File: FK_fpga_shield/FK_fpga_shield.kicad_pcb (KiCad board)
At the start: 2 copper layers, 136 parts, among them J0 USB_B_Mini, J1 molex-51382-0400-microclasp, J10 molex-51382-0400-microclasp, J11 molex-51382-0400-microclasp, J12 molex-51382-0400-microclasp, J13 molex-51382-0400-microclasp, J14 molex-51382-0400-microclasp, J15 molex-51382-0400-microclasp, J16 molex-51382-0400-microclasp, J17 molex-51382-0400-microclasp, J18 molex-51382-0400-microclasp, J19 molex-51382-0400-microclasp, J2 molex-51382-0400-microclasp, J20 molex-51382-0400-microclasp, J21 molex-51382-0400-microclasp, J22 molex-51382-0400-microclasp, J23 molex-51382-0400-microclasp, J24 molex-51382-0400-microclasp, J25 molex-51382-0400-microclasp, J26 molex-51382-0400-microclasp, J27 molex-51382-0400-microclasp, J28 molex-51382-0400-microclasp, J29 molex-51382-0400-microclasp, J3 molex-51382-0400-microclasp, J30 molex-51382-0400-microclasp, J31 molex-51382-0400-microclasp, J32 molex-51382-0400-microclasp, J33 molex-51382-0400-microclasp, J34 molex-51382-0400-microclasp, J35 molex-51382-0400-microclasp, J4 molex-51382-0400-microclasp, J5 molex-51382-0400-microclasp, J6 molex-51382-0400-microclasp, J7 molex-51382-0400-microclasp, J8 molex-51382-0400-microclasp, J9 molex-51382-0400-microclasp, U1 FT232RL, U2 nvt2010pw, U3 nvt2010pw, U4 nvt2010pw, U5 nvt2010pw, U6 nvt2010pw, U7 nvt2010pw, U8 nvt2010pw

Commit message: wip lazyour (mapped to header)
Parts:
- removed the J11 at (221.2, 43.8)
- added J15: molex-51382-0400-microclasp, FK_fpga_shield_custom_footprints:Molex_MicroClasp_55935-0410_1x04_P2.00mm_Horizontal_3DMODEL, F.Cu at (247.0, 65.2)
- moved C6 349.4 mm to (345.1, 24.9)
- moved R79 349.4 mm to (349.9, 33.7)
- moved C2 349.4 mm to (360.3, 55.8)
- moved C4 349.4 mm to (365.1, 55.8)
- moved C7 349.4 mm to (334.1, 35.7)
- moved C8 349.4 mm to (329.4, 38.6)
- moved R54 349.4 mm to (348.4, 36.6)
- moved C9 298.0 mm to (345.2, -20.8)
- moved R53 298.0 mm to (345.2, -26.7)
- moved U4 274.0 mm to (214.4, 68.4), turned to 45 degrees
- moved C10 263.0 mm to (293.4, 9.55)
- moved C11 263.0 mm to (288.6, 12.5)
- moved C5 263.0 mm to (293.4, 15.4)
- moved R55 263.0 mm to (293.4, 21.4)
- moved R57 263.0 mm to (302.9, 17.1)
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- renumbered J15 to J11, J14 to J12, J12 to J14
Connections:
- H1 pad 13: Net-(H1-Pad13) -> /6b
- H1 pad 14: Net-(H1-Pad14) -> /6a
- H1 pad 15: Net-(H1-Pad15) -> /7b
- H1 pad 16: Net-(H1-Pad16) -> /7a
- H1 pad 17: Net-(H1-Pad17) -> /8b
- H1 pad 18: Net-(H1-Pad18) -> /8a
- H1 pad 19: Net-(H1-Pad19) -> /9b
- H1 pad 20: Net-(H1-Pad20) -> /9a
- H1 pad 21: Net-(H1-Pad21) -> /10b
- H1 pad 22: Net-(H1-Pad22) -> /10a
- H1 pad 23: Net-(H1-Pad23) -> /11b
- H1 pad 24: Net-(H1-Pad24) -> /11a
- H1 pad 25: Net-(H1-Pad25) -> /12b
- H1 pad 26: Net-(H1-Pad26) -> /12a
- H1 pad 27: Net-(H1-Pad27) -> /13b
- H1 pad 28: Net-(H1-Pad28) -> /13a
- H1 pad 31: Net-(H1-Pad31) -> /14b
- H1 pad 32: Net-(H1-Pad32) -> /14a
- H1 pad 33: Net-(H1-Pad33) -> /15b
- H1 pad 34: Net-(H1-Pad34) -> /15a
- H1 pad 35: Net-(H1-Pad35) -> /16b
- H1 pad 36: Net-(H1-Pad36) -> /16a
- H1 pad 37: Net-(H1-Pad37) -> /17b
- H1 pad 38: Net-(H1-Pad38) -> /17a
- H1 pad 39: Net-(H1-Pad39) -> /18b
- H1 pad 40: Net-(H1-Pad40) -> /18a
- H2 pad 1: Net-(H2-Pad1) -> /19b
- H2 pad 10: Net-(H2-Pad10) -> /23a
- H2 pad 13: Net-(H2-Pad13) -> /24b
- H2 pad 14: Net-(H2-Pad14) -> /24a
- H2 pad 15: Net-(H2-Pad15) -> /25b
- H2 pad 16: Net-(H2-Pad16) -> /25a
- H2 pad 17: Net-(H2-Pad17) -> /26b
- H2 pad 18: Net-(H2-Pad18) -> /26a
- H2 pad 19: Net-(H2-Pad19) -> /27b
- H2 pad 2: Net-(H2-Pad2) -> /19a
- H2 pad 20: Net-(H2-Pad20) -> /27a
- H2 pad 21: Net-(H2-Pad21) -> /28b
- H2 pad 22: Net-(H2-Pad22) -> /28a
- H2 pad 23: Net-(H2-Pad23) -> /29b
- H2 pad 24: Net-(H2-Pad24) -> /29a
- H2 pad 25: Net-(H2-Pad25) -> /30b
- H2 pad 26: Net-(H2-Pad26) -> /30a
- H2 pad 27: Net-(H2-Pad27) -> /31b
- H2 pad 28: Net-(H2-Pad28) -> /31a
- H2 pad 3: Net-(H2-Pad3) -> /20b
- H2 pad 31: Net-(H2-Pad31) -> /32b
- H2 pad 32: Net-(H2-Pad32) -> /32a
- H2 pad 33: Net-(H2-Pad33) -> /33b
- H2 pad 34: Net-(H2-Pad34) -> /33a
- H2 pad 35: Net-(H2-Pad35) -> /34b
- H2 pad 36: Net-(H2-Pad36) -> /34a
- H2 pad 37: Net-(H2-Pad37) -> /35b
- H2 pad 38: Net-(H2-Pad38) -> /35a
- H2 pad 39: Net-(H2-Pad39) -> /TX
- H2 pad 4: Net-(H2-Pad4) -> /20a
- H2 pad 40: Net-(H2-Pad40) -> /RX
- H2 pad 5: Net-(H2-Pad5) -> /21b
- H2 pad 6: Net-(H2-Pad6) -> /21a
- H2 pad 7: Net-(H2-Pad7) -> /22b
- H2 pad 8: Net-(H2-Pad8) -> /22a
- H2 pad 9: Net-(H2-Pad9) -> /23b
- R11 pad 2: Net-(J16-Pad4) -> Net-(J20-Pad4)
- R12 pad 2: Net-(J21-Pad4) -> Net-(J25-Pad4)
- R16 pad 2: Net-(J17-Pad2) -> Net-(J19-Pad2)
- R17 pad 2: Net-(J22-Pad2) -> Net-(J24-Pad2)
- R21 pad 2: Net-(J17-Pad4) -> Net-(J19-Pad4)
- R22 pad 2: Net-(J22-Pad4) -> Net-(J24-Pad4)
- R36 pad 2: Net-(J19-Pad2) -> Net-(J17-Pad2)
- R37 pad 2: Net-(J24-Pad2) -> Net-(J22-Pad2)
- R41 pad 2: Net-(J19-Pad4) -> Net-(J17-Pad4)
- R42 pad 2: Net-(J24-Pad4) -> Net-(J22-Pad4)
- R46 pad 2: Net-(J20-Pad2) -> Net-(J16-Pad2)
- R47 pad 2: Net-(J25-Pad2) -> Net-(J21-Pad2)
- R51 pad 2: Net-(J20-Pad4) -> Net-(J16-Pad4)
- R52 pad 2: Net-(J25-Pad4) -> Net-(J21-Pad4)
- R58 pad 2: Net-(J26-Pad2) -> Net-(J30-Pad2)
- R59 pad 2: Net-(J31-Pad2) -> Net-(J35-Pad2)
- R6 pad 2: Net-(J16-Pad2) -> Net-(J20-Pad2)
- R60 pad 2: Net-(J26-Pad4) -> Net-(J30-Pad4)
- R61 pad 2: Net-(J31-Pad4) -> Net-(J35-Pad4)
- R62 pad 2: Net-(J27-Pad2) -> Net-(J29-Pad2)
- R63 pad 2: Net-(J32-Pad2) -> Net-(J34-Pad2)
- R64 pad 2: Net-(J27-Pad4) -> Net-(J29-Pad4)
- R65 pad 2: Net-(J32-Pad4) -> Net-(J34-Pad4)
- R7 pad 2: Net-(J21-Pad2) -> Net-(J25-Pad2)
- R70 pad 2: Net-(J29-Pad2) -> Net-(J27-Pad2)
- R71 pad 2: Net-(J34-Pad2) -> Net-(J32-Pad2)
- R72 pad 2: Net-(J29-Pad4) -> Net-(J27-Pad4)
- R73 pad 2: Net-(J34-Pad4) -> Net-(J32-Pad4)
- R74 pad 2: Net-(J30-Pad2) -> Net-(J26-Pad2)
- R75 pad 2: Net-(J35-Pad2) -> Net-(J31-Pad2)
- R76 pad 2: Net-(J30-Pad4) -> Net-(J26-Pad4)
- R77 pad 2: Net-(J35-Pad4) -> Net-(J31-Pad4)
- U3 pad 10: Net-(U3-Pad10) -> /9a
- U3 pad 11: Net-(U3-Pad11) -> /10b
- U3 pad 12: Net-(U3-Pad12) -> /10a
- U3 pad 3: Net-(U3-Pad3) -> /6b
- U3 pad 4: Net-(U3-Pad4) -> /6a
- U3 pad 5: Net-(U3-Pad5) -> /7b
- U3 pad 6: Net-(U3-Pad6) -> /7a
- U3 pad 7: Net-(U3-Pad7) -> /8b
- U3 pad 8: Net-(U3-Pad8) -> /8a
- U3 pad 9: Net-(U3-Pad9) -> /9b
- U4 pad 10: Net-(U4-Pad10) -> /14a
- U4 pad 11: Net-(U4-Pad11) -> /15b
- U4 pad 12: Net-(U4-Pad12) -> /15a
- U4 pad 3: Net-(U4-Pad3) -> /11b
- U4 pad 4: Net-(U4-Pad4) -> /11a
- U4 pad 5: Net-(U4-Pad5) -> /12b
- U4 pad 6: Net-(U4-Pad6) -> /12a
- U4 pad 7: Net-(U4-Pad7) -> /13b
- U4 pad 8: Net-(U4-Pad8) -> /13a
- U4 pad 9: Net-(U4-Pad9) -> /14b
- U5 pad 10: Net-(U5-Pad10) -> /19a
- U5 pad 11: Net-(U5-Pad11) -> /20b
- U5 pad 12: Net-(U5-Pad12) -> /20a
- U5 pad 13: Net-(J16-Pad2) -> Net-(J20-Pad2)
- U5 pad 14: Net-(J16-Pad4) -> Net-(J20-Pad4)
- U5 pad 15: Net-(J17-Pad2) -> Net-(J19-Pad2)
- U5 pad 16: Net-(J17-Pad4) -> Net-(J19-Pad4)
- U5 pad 19: Net-(J19-Pad2) -> Net-(J17-Pad2)
- U5 pad 20: Net-(J19-Pad4) -> Net-(J17-Pad4)
- U5 pad 21: Net-(J20-Pad2) -> Net-(J16-Pad2)
- U5 pad 22: Net-(J20-Pad4) -> Net-(J16-Pad4)
- U5 pad 3: Net-(U5-Pad3) -> /16b
- U5 pad 4: Net-(U5-Pad4) -> /16a
- U5 pad 5: Net-(U5-Pad5) -> /17b
- U5 pad 6: Net-(U5-Pad6) -> /17a
- U5 pad 7: Net-(U5-Pad7) -> /18b
- U5 pad 8: Net-(U5-Pad8) -> /18a
- U5 pad 9: Net-(U5-Pad9) -> /19b
- U6 pad 10: Net-(U6-Pad10) -> /24a
- U6 pad 11: Net-(U6-Pad11) -> /25b
- U6 pad 12: Net-(U6-Pad12) -> /25a
- U6 pad 13: Net-(J21-Pad2) -> Net-(J25-Pad2)
- U6 pad 14: Net-(J21-Pad4) -> Net-(J25-Pad4)
- U6 pad 15: Net-(J22-Pad2) -> Net-(J24-Pad2)
- U6 pad 16: Net-(J22-Pad4) -> Net-(J24-Pad4)
- U6 pad 19: Net-(J24-Pad2) -> Net-(J22-Pad2)
- U6 pad 20: Net-(J24-Pad4) -> Net-(J22-Pad4)
- U6 pad 21: Net-(J25-Pad2) -> Net-(J21-Pad2)
- U6 pad 22: Net-(J25-Pad4) -> Net-(J21-Pad4)
- U6 pad 3: Net-(U6-Pad3) -> /21b
- U6 pad 4: Net-(U6-Pad4) -> /21a
- U6 pad 5: Net-(U6-Pad5) -> /22b
- U6 pad 6: Net-(U6-Pad6) -> /22a
- U6 pad 7: Net-(U6-Pad7) -> /23b
- U6 pad 8: Net-(U6-Pad8) -> /23a
- U6 pad 9: Net-(U6-Pad9) -> /24b
- U7 pad 10: Net-(U7-Pad10) -> /29a
- U7 pad 11: Net-(U7-Pad11) -> /30b
- U7 pad 12: Net-(U7-Pad12) -> /30a
- U7 pad 13: Net-(J26-Pad2) -> Net-(J30-Pad2)
- U7 pad 14: Net-(J26-Pad4) -> Net-(J30-Pad4)
- U7 pad 15: Net-(J27-Pad2) -> Net-(J29-Pad2)
- U7 pad 16: Net-(J27-Pad4) -> Net-(J29-Pad4)
- U7 pad 19: Net-(J29-Pad2) -> Net-(J27-Pad2)
- U7 pad 20: Net-(J29-Pad4) -> Net-(J27-Pad4)
- U7 pad 21: Net-(J30-Pad2) -> Net-(J26-Pad2)
- U7 pad 22: Net-(J30-Pad4) -> Net-(J26-Pad4)
- U7 pad 3: Net-(U7-Pad3) -> /26b
- U7 pad 4: Net-(U7-Pad4) -> /26a
- U7 pad 5: Net-(U7-Pad5) -> /27b
- U7 pad 6: Net-(U7-Pad6) -> /27a
- U7 pad 7: Net-(U7-Pad7) -> /28b
- U7 pad 8: Net-(U7-Pad8) -> /28a
- U7 pad 9: Net-(U7-Pad9) -> /29b
- U8 pad 10: Net-(U8-Pad10) -> /34a
- U8 pad 11: Net-(U8-Pad11) -> /35b
- U8 pad 12: Net-(U8-Pad12) -> /35a
- U8 pad 13: Net-(J31-Pad2) -> Net-(J35-Pad2)
- U8 pad 14: Net-(J31-Pad4) -> Net-(J35-Pad4)
- U8 pad 15: Net-(J32-Pad2) -> Net-(J34-Pad2)
- U8 pad 16: Net-(J32-Pad4) -> Net-(J34-Pad4)
- U8 pad 19: Net-(J34-Pad2) -> Net-(J32-Pad2)
- U8 pad 20: Net-(J34-Pad4) -> Net-(J32-Pad4)
- U8 pad 21: Net-(J35-Pad2) -> Net-(J31-Pad2)
- U8 pad 22: Net-(J35-Pad4) -> Net-(J31-Pad4)
- U8 pad 3: Net-(U8-Pad3) -> /31b
- U8 pad 4: Net-(U8-Pad4) -> /31a
- U8 pad 5: Net-(U8-Pad5) -> /32b
- U8 pad 6: Net-(U8-Pad6) -> /32a
- U8 pad 7: Net-(U8-Pad7) -> /33b
- U8 pad 8: Net-(U8-Pad8) -> /33a
- U8 pad 9: Net-(U8-Pad9) -> /34b
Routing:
- net Net-(J1-Pad4): track 33.7 -> 0.00 mm
- net Net-(J5-Pad2): track 30.7 -> 0.00 mm
- net Net-(J1-Pad2): track 29.3 -> 0.00 mm
- net /5V: track 28.8 -> 0.00 mm
- net Net-(J5-Pad4): track 26.8 -> 0.00 mm
- net Net-(J2-Pad4): track 24.0 -> 0.00 mm
- net Net-(J4-Pad2): track 20.7 -> 0.00 mm
- net Net-(J2-Pad2): track 20.1 -> 0.00 mm
- net Net-(J4-Pad4): track 16.5 -> 0.00 mm
- net GND: track 0.00 -> 15.4 mm, vias 0 -> 1
- net Net-(J3-Pad4): track 14.8 -> 0.00 mm
- net Net-(J3-Pad2): track 13.4 -> 0.00 mm
- net Net-(J0-Pad2): track 0.00 -> 12.8 mm
- net Net-(J0-Pad3): track 0.00 -> 6.74 mm
- net Net-(R1-Pad2): track 0.00 -> 5.59 mm
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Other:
- board outline added: 182.2 x 125 mm

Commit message: wip
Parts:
- moved R53 278.2 mm to (82.0, 63.2)
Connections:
- H2 pad 39: /TX -> /RX
- H2 pad 40: /RX -> /TX
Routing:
- net Net-(J14-Pad2): track 0.00 -> 37.6 mm
- net Net-(J1-Pad4): track 0.00 -> 33.2 mm
- net Net-(J14-Pad4): track 0.00 -> 32.0 mm
- net Net-(J1-Pad2): track 0.00 -> 29.2 mm
- net Net-(J15-Pad4): track 0.00 -> 28.2 mm
- net Net-(J6-Pad4): track 0.00 -> 28.0 mm
- net Net-(J5-Pad2): track 0.00 -> 26.1 mm
- net Net-(J10-Pad2): track 0.00 -> 26.0 mm
- net Net-(J15-Pad2): track 0.00 -> 25.3 mm
- net Net-(J13-Pad2): track 0.00 -> 25.2 mm
- net Net-(J6-Pad2): track 0.00 -> 22.9 mm
- net Net-(J5-Pad4): track 0.00 -> 21.4 mm
- net Net-(J10-Pad4): track 0.00 -> 21.3 mm
- net Net-(J13-Pad4): track 0.00 -> 19.2 mm
- net Net-(J2-Pad4): track 0.00 -> 18.6 mm
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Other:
- copper layers 2 -> 4

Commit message: wip route before U4,U6 move
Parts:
- moved R56 21.9 mm to (212.5, 89.8)
- moved R42 9.15 mm to (242.3, 143.2), turned to 45 degrees
- moved R15 7.74 mm to (242.0, 57.3), turned to 315 degrees
- moved R37 6.68 mm to (239.6, 145.9), turned to 225 degrees
- moved R20 5.59 mm to (239.3, 54.6), turned to 135 degrees
- moved U4 5.55 mm to (216.8, 73.4)
- moved U6 5.55 mm to (216.6, 129.4)
- moved R14 4.25 mm to (180.1, 53.1)
- moved R19 4.25 mm to (176.2, 53.1)
- moved R24 4.25 mm to (170.1, 53.0)
- moved R29 4.25 mm to (166.2, 53.0)
- moved R34 4.25 mm to (159.4, 53.0)
- moved R39 4.25 mm to (155.7, 53.0)
- moved R4 4.25 mm to (193.7, 53.1)
- moved R44 4.25 mm to (147.0, 53.0)
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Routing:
- net /1b: track 0.00 -> 53.5 mm
- net /2b: track 0.00 -> 51.5 mm
- net /5b: track 0.00 -> 51.4 mm
- net /1a: track 0.00 -> 49.9 mm
- net /3b: track 0.00 -> 49.5 mm
- net /4b: track 0.00 -> 49.3 mm
- net /5a: track 0.00 -> 49.2 mm
- net /4a: track 0.00 -> 47.2 mm
- net /2a: track 0.00 -> 46.8 mm
- net /3a: track 0.00 -> 46.0 mm
- net Net-(J16-Pad4): track 0.00 -> 36.1 mm
- net Net-(J16-Pad2): track 0.00 -> 31.8 mm
- net Net-(J20-Pad2): track 0.00 -> 31.3 mm
- net Net-(J31-Pad4): track 0.00 -> 29.4 mm
- net Net-(J26-Pad4): track 0.00 -> 28.7 mm
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
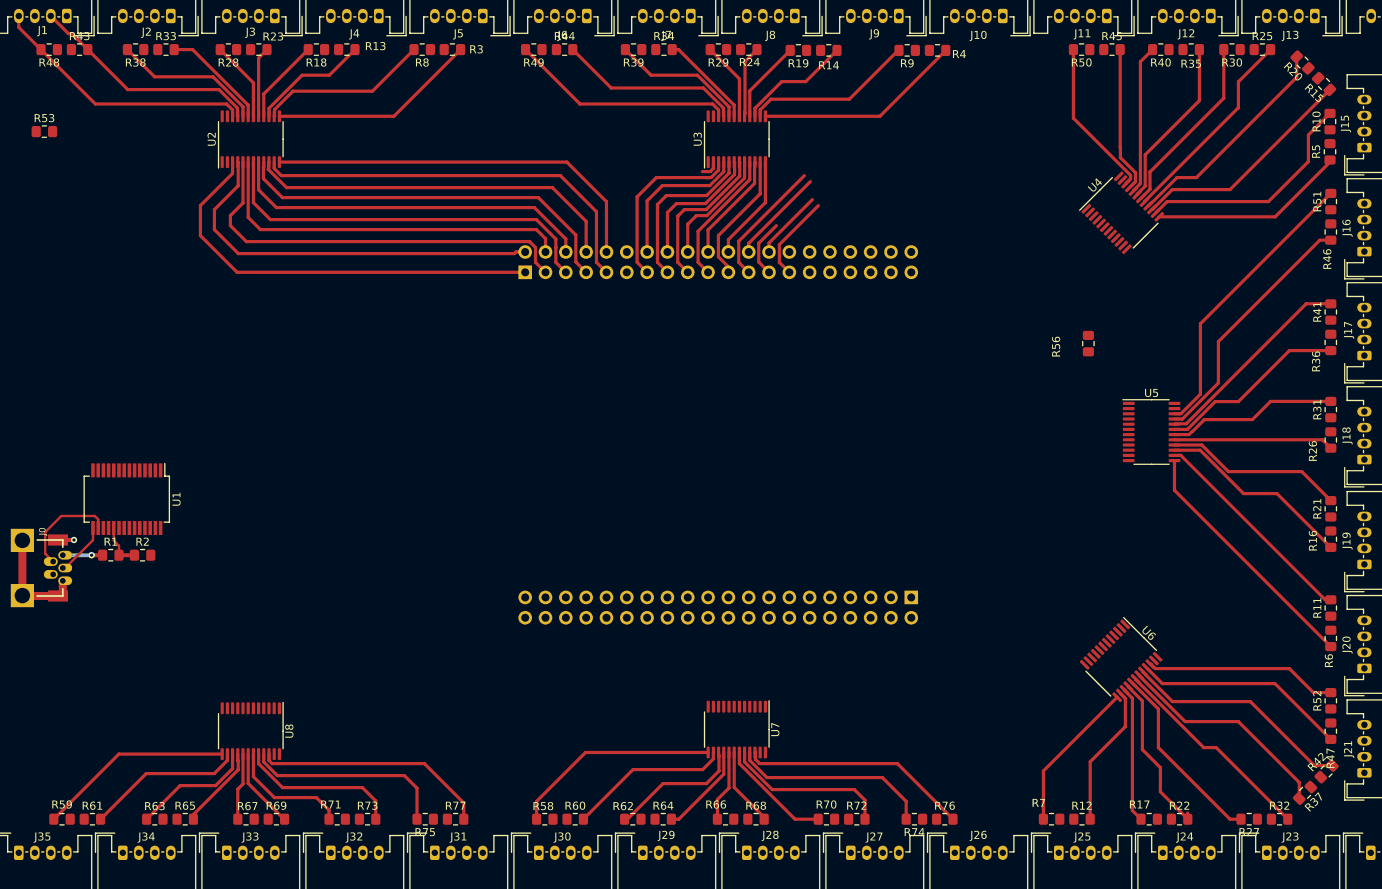
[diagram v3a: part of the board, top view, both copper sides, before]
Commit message: levelshifter to fpga signals routed
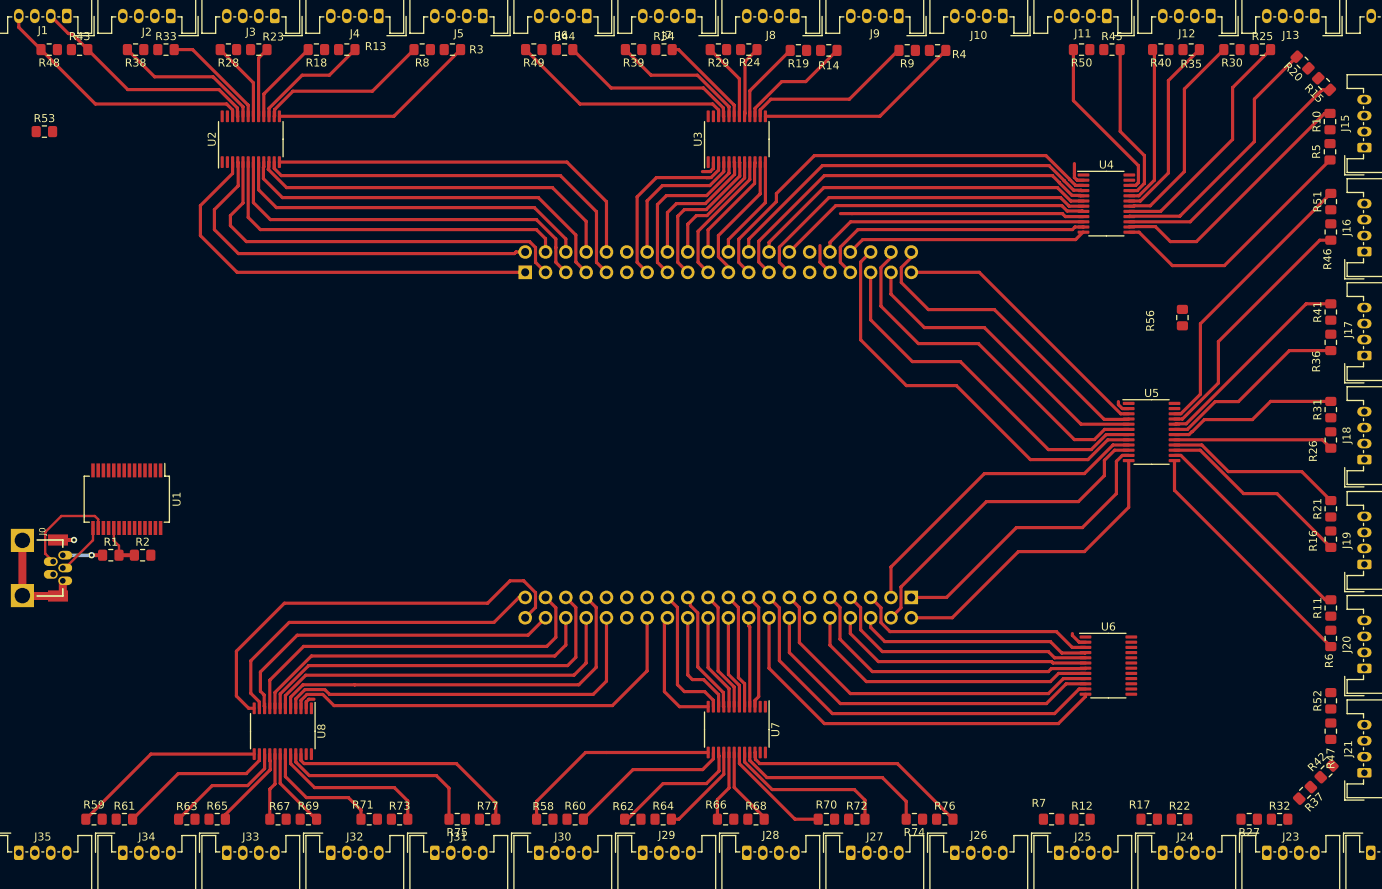
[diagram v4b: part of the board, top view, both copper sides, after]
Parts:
- moved R56 12.2 mm to (224.2, 86.5)
- moved R59 4.00 mm to (88.2, 149.2)
- moved R61 4.00 mm to (92.0, 149.2)
- moved R63 4.00 mm to (99.8, 149.2)
- moved R65 4.00 mm to (103.6, 149.2)
- moved R67 4.00 mm to (111.2, 149.2)
- moved R69 4.00 mm to (115.0, 149.2)
- moved R71 4.00 mm to (122.6, 149.2)
- moved R73 4.00 mm to (126.4, 149.2)
- moved R75 4.00 mm to (133.6, 149.2)
- moved R77 4.00 mm to (137.4, 149.2)
- moved U8 4.00 mm to (111.8, 138.2)
- moved U4 2.35 mm to (214.8, 72.2), turned to 0 degrees
- moved U6 1.71 mm to (215.0, 130.0), turned to 0 degrees
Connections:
- H1 pad 35: /16b -> /18b
- H1 pad 36: /16a -> /18a
- H1 pad 39: /18b -> /16b
- H1 pad 40: /18a -> /16a
- H2 pad 1: /19b -> /20b
- H2 pad 2: /19a -> /20a
- H2 pad 27: /31b -> /RX
- H2 pad 28: /31a -> /31b
- H2 pad 3: /20b -> /19b
- H2 pad 31: /32b -> /TX
- H2 pad 32: /32a -> /31a
- H2 pad 33: /33b -> /32b
- H2 pad 34: /33a -> /32a
- H2 pad 35: /34b -> /33b
- H2 pad 36: /34a -> /33a
- H2 pad 37: /35b -> /34b
- H2 pad 38: /35a -> /34a
- H2 pad 39: /RX -> /35b
- H2 pad 4: /20a -> /19a
- H2 pad 40: /TX -> /35a
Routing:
- net /35a: track 0.00 -> 54.3 mm
- net /31b: track 0.00 -> 53.6 mm
- net /18a: track 0.00 -> 52.2 mm
- net /25b: track 0.00 -> 50.7 mm
- net /25a: track 0.00 -> 50.4 mm
- net /32b: track 0.00 -> 50.4 mm
- net /31a: track 0.00 -> 49.4 mm
- net /33b: track 0.00 -> 48.6 mm
- net /34b: track 0.00 -> 47.0 mm
- net /32a: track 0.00 -> 46.5 mm
- net /18b: track 0.00 -> 45.7 mm
- net /17a: track 0.00 -> 45.7 mm
- net /24b: track 0.00 -> 45.3 mm
- net /24a: track 0.00 -> 45.0 mm
- net /33a: track 0.00 -> 44.2 mm
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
